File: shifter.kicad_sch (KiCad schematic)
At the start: 11 parts

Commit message: made the board double wide. rough ASIC and vreg placement.
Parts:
- D1: renamed from D3; symbol Device:D -> bitaxe:D
- D2: renamed from D1; symbol Device:D -> bitaxe:D
- D3: renamed from D4; symbol Device:D -> bitaxe:D
- D4: renamed from D2; symbol Device:D -> bitaxe:D
- renumbered C to C180, R29 to R33, R14 to R34, R32 to R35, R26 to R36, R27 to R37, R28 to R38
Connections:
- net RESET_IN: now also D3.A; no longer D3.2 (A)
- net RESET_OUT: now also D3.K; no longer D3.1 (K)
- net RX_IN: now also D4.A; no longer D4.2 (A)
- net RX_OUT: now also D4.K; no longer D4.1 (K)
- net TRIP_IN: now also D1.K; no longer D1.1 (K)
- net TRIP_OUT: now also D1.A; no longer D1.2 (A)
- net TX_IN: now also D2.K; no longer D2.1 (K)
- net TX_OUT: now also D2.A; no longer D2.2 (A)
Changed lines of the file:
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@@
 		(on_board yes)
 		(dnp no)
-		(property "Reference" "R29"
+		(property "Reference" "R33"
 			(at 102.87 111.76 0)
 			(effects
@@
 			(project "BitaxeBonanza"
 				(path "/61fe8d2c-9301-4ad9-8caf-c47acfa835b0/5053a6d5-ae8d-4ae0-9f6e-0d65e80da719/0ebdc3ac-b196-4195-a4b9-cad7cca42700"
-					(reference "R29")
+					(reference "R33")
 					(unit 1)
 				)
 				(path "/61fe8d2c-9301-4ad9-8caf-c47acfa835b0/5053a6d5-ae8d-4ae0-9f6e-0d65e80da719/a86c111d-117d-4919-aa69-a196b04aa4d8"
-					(reference "R34")
+					(reference "R39")
 					(unit 1)
 				)
@@
 	)
 	(symbol
-		(lib_id "Device:D")
+		(lib_id "bitaxe:D")
 		(at 162.56 83.82 90)
 		(unit 1)
@@
 		(on_board yes)
 		(dnp no)
-		(property "Reference" "D2"
+		(property "Reference" "D4"
 			(at 161.29 80.518 0)
 			(effects
@@
 			)
 		)
-		(property "Datasheet" "https://fscdn.rohm.com/en/products/databook/datasheet/discrete/diode/switching/1ss380vmte-17-e.pdf"
+		(property "Datasheet" "~"
 			(at 162.56 83.82 0)
 			(effects
@@
 			)
 		)
-		(pin "1"
-		)
-		(pin "2"
-		)
-		(instances
-			(project "BitaxeBonanza"
-				(path "/61fe8d2c-9301-4ad9-8caf-c47acfa835b0/5053a6d5-ae8d-4ae0-9f6e-0d65e80da719/0ebdc3ac-b196-4195-a4b9-cad7cca42700"
-					(reference "D2")
+		(property "Sim.Device" "D"
+			(at 162.56 83.82 0)
+			(effects
+				(font
+					(size 1.27 1.27)
+				)
+				(hide yes)
+			)
+		)
+		(property "Sim.Pins" "1=K 2=A"
+			(at 162.56 83.82 0)
+			(effects
+				(font
+					(size 1.27 1.27)
+				)
+				(hide yes)
+			)
+		)
+		(pin "A"
+		)
+		(pin "K"
+		)
+		(instances
+			(project "BitaxeBonanza"
+				(path "/61fe8d2c-9301-4ad9-8caf-c47acfa835b0/5053a6d5-ae8d-4ae0-9f6e-0d65e80da719/0ebdc3ac-b196-4195-a4b9-cad7cca42700"
+					(reference "D4")
 					(unit 1)
 				)
@@
 		(dnp no)
 		(fields_autoplaced yes)
-		(property "Reference" "C"
+		(property "Reference" "C180"
 			(at 190.5 91.4335 0)
 			(effects
@@
 		(instances
 			(project "BitaxeBonanza"
+				(path "/61fe8d2c-9301-4ad9-8caf-c47acfa835b0/5053a6d5-ae8d-4ae0-9f6e-0d65e80da719/0ebdc3ac-b196-4195-a4b9-cad7cca42700"
+					(reference "C180")
+					(unit 1)
+				)
 				(path "/61fe8d2c-9301-4ad9-8caf-c47acfa835b0/5053a6d5-ae8d-4ae0-9f6e-0d65e80da719/a86c111d-117d-4919-aa69-a196b04aa4d8"
-					(reference "C50")
+					(reference "C181")
 					(unit 1)
 				)
 				(path "/61fe8d2c-9301-4ad9-8caf-c47acfa835b0/5053a6d5-ae8d-4ae0-9f6e-0d65e80da719/aedf8646-f124-43c2-a6e9-f307494e235d"
-					(reference "C51")
+					(reference "C182")
 					(unit 1)
 				)
@@
 		(on_board yes)
 		(dnp no)
-		(property "Reference" "R28"
+		(property "Reference" "R38"
 			(at 197.866 68.326 90)
 			(effects
@@
 			(project "BitaxeBonanza"
 				(path "/61fe8d2c-9301-4ad9-8caf-c47acfa835b0/5053a6d5-ae8d-4ae0-9f6e-0d65e80da719/0ebdc3ac-b196-4195-a4b9-cad7cca42700"
-					(reference "R28")
+					(reference "R38")
 					(unit 1)
 				)
@@
 	)
 	(symbol
-		(lib_id "Device:D")
+		(lib_id "bitaxe:D")
 		(at 93.98 83.82 90)
 		(unit 1)
@@
 		(on_board yes)
 		(dnp no)
-		(property "Reference" "D3"
+		(property "Reference" "D1"
 			(at 96.266 79.756 0)
 			(effects
@@
 			)
 		)
-		(property "Datasheet" "https://fscdn.rohm.com/en/products/databook/datasheet/discrete/diode/switching/1ss380vmte-17-e.pdf"
+		(property "Datasheet" "~"
 			(at 93.98 83.82 0)
 			(effects
@@
 			)
 		)
-		(pin "1"
-		)
-		(pin "2"
-		)
-		(instances
-			(project "BitaxeBonanza"
-				(path "/61fe8d2c-9301-4ad9-8caf-c47acfa835b0/5053a6d5-ae8d-4ae0-9f6e-0d65e80da719/0ebdc3ac-b196-4195-a4b9-cad7cca42700"
-					(reference "D3")
+		(property "Sim.Device" "D"
+			(at 93.98 83.82 0)
+			(effects
+				(font
+					(size 1.27 1.27)
+				)
+				(hide yes)
+			)
+		)
+		(property "Sim.Pins" "1=K 2=A"
+			(at 93.98 83.82 0)
+			(effects
+				(font
+					(size 1.27 1.27)
+				)
+				(hide yes)
+			)
+		)
+		(pin "A"
+		)
+		(pin "K"
+		)
+		(instances
+			(project "BitaxeBonanza"
+				(path "/61fe8d2c-9301-4ad9-8caf-c47acfa835b0/5053a6d5-ae8d-4ae0-9f6e-0d65e80da719/0ebdc3ac-b196-4195-a4b9-cad7cca42700"
+					(reference "D1")
 					(unit 1)
 				)
@@
 		(on_board yes)
 		(dnp no)
-		(property "Reference" "R14"
+		(property "Reference" "R34"
 			(at 120.65 91.186 0)
 			(effects
@@
 			(project "BitaxeBonanza"
 				(path "/61fe8d2c-9301-4ad9-8caf-c47acfa835b0/5053a6d5-ae8d-4ae0-9f6e-0d65e80da719/0ebdc3ac-b196-4195-a4b9-cad7cca42700"
-					(reference "R14")
+					(reference "R34")
 					(unit 1)
 				)
 				(path "/61fe8d2c-9301-4ad9-8caf-c47acfa835b0/5053a6d5-ae8d-4ae0-9f6e-0d65e80da719/a86c111d-117d-4919-aa69-a196b04aa4d8"
-					(reference "R36")
+					(reference "R40")
 					(unit 1)
 				)
@@
 	)
 	(symbol
-		(lib_id "Device:D")
+		(lib_id "bitaxe:D")
 		(at 139.7 83.82 90)
 		(unit 1)
@@
 		(on_board yes)
 		(dnp no)
-		(property "Reference" "D4"
+		(property "Reference" "D3"
 			(at 141.478 80.518 0)
 			(effects
@@
 			)
 		)
-		(property "Datasheet" "https://fscdn.rohm.com/en/products/databook/datasheet/discrete/diode/switching/1ss380vmte-17-e.pdf"
+		(property "Datasheet" "~"
 			(at 139.7 83.82 0)
 			(effects
@@
 			)
 		)
-		(pin "1"
-		)
-		(pin "2"
-		)
-		(instances
-			(project "BitaxeBonanza"
-				(path "/61fe8d2c-9301-4ad9-8caf-c47acfa835b0/5053a6d5-ae8d-4ae0-9f6e-0d65e80da719/0ebdc3ac-b196-4195-a4b9-cad7cca42700"
-					(reference "D4")
+		(property "Sim.Device" "D"
+			(at 139.7 83.82 0)
+			(effects
+				(font
+					(size 1.27 1.27)
+				)
+				(hide yes)
+			)
+		)
+		(property "Sim.Pins" "1=K 2=A"
+			(at 139.7 83.82 0)
+			(effects
+				(font
+					(size 1.27 1.27)
+				)
+				(hide yes)
+			)
+		)
+		(pin "K"
+		)
+		(pin "A"
+		)
+		(instances
+			(project "BitaxeBonanza"
+				(path "/61fe8d2c-9301-4ad9-8caf-c47acfa835b0/5053a6d5-ae8d-4ae0-9f6e-0d65e80da719/0ebdc3ac-b196-4195-a4b9-cad7cca42700"
+					(reference "D3")
 					(unit 1)
 				)
@@
 		(on_board yes)
 		(dnp no)
-		(property "Reference" "R32"
+		(property "Reference" "R35"
 			(at 145.034 66.04 0)
 			(effects
@@
 			(project "BitaxeBonanza"
 				(path "/61fe8d2c-9301-4ad9-8caf-c47acfa835b0/5053a6d5-ae8d-4ae0-9f6e-0d65e80da719/0ebdc3ac-b196-4195-a4b9-cad7cca42700"
-					(reference "R32")
+					(reference "R35")
 					(unit 1)
 				)
@@
 	)
 	(symbol
-		(lib_id "Device:D")
+		(lib_id "bitaxe:D")
 		(at 128.27 83.82 90)
 		(unit 1)
@@
 		(on_board yes)
 		(dnp no)
-		(property "Reference" "D1"
+		(property "Reference" "D2"
 			(at 130.048 80.01 0)
 			(effects
@@
 			)
 		)
-		(property "Datasheet" "https://fscdn.rohm.com/en/products/databook/datasheet/discrete/diode/switching/1ss380vmte-17-e.pdf"
+		(property "Datasheet" "~"
 			(at 128.27 83.82 0)
 			(effects
@@
 			)
 		)
-		(pin "1"
-		)
-		(pin "2"
-		)
-		(instances
-			(project "BitaxeBonanza"
-				(path "/61fe8d2c-9301-4ad9-8caf-c47acfa835b0/5053a6d5-ae8d-4ae0-9f6e-0d65e80da719/0ebdc3ac-b196-4195-a4b9-cad7cca42700"
-					(reference "D1")
+		(property "Sim.Device" "D"
+			(at 128.27 83.82 0)
+			(effects
+				(font
+					(size 1.27 1.27)
+				)
+				(hide yes)
+			)
+		)
+		(property "Sim.Pins" "1=K 2=A"
+			(at 128.27 83.82 0)
+			(effects
+				(font
+					(size 1.27 1.27)
+				)
+				(hide yes)
+			)
+		)
+		(pin "K"
+		)
+		(pin "A"
+		)
+		(instances
+			(project "BitaxeBonanza"
+				(path "/61fe8d2c-9301-4ad9-8caf-c47acfa835b0/5053a6d5-ae8d-4ae0-9f6e-0d65e80da719/0ebdc3ac-b196-4195-a4b9-cad7cca42700"
+					(reference "D2")
 					(unit 1)
 				)
@@
 		(on_board yes)
 		(dnp no)
-		(property "Reference" "R26"
+		(property "Reference" "R36"
 			(at 167.894 66.04 0)
 			(effects
@@
 			(project "BitaxeBonanza"
 				(path "/61fe8d2c-9301-4ad9-8caf-c47acfa835b0/5053a6d5-ae8d-4ae0-9f6e-0d65e80da719/0ebdc3ac-b196-4195-a4b9-cad7cca42700"
-					(reference "R26")
+					(reference "R36")
 					(unit 1)
 				)
@@
 		(on_board yes)
 		(dnp no)
-		(property "Reference" "R27"
+		(property "Reference" "R37"
 			(at 198.12 50.8 90)
 			(effects
@@
 			(project "BitaxeBonanza"
 				(path "/61fe8d2c-9301-4ad9-8caf-c47acfa835b0/5053a6d5-ae8d-4ae0-9f6e-0d65e80da719/0ebdc3ac-b196-4195-a4b9-cad7cca42700"
-					(reference "R27")
-					(unit 1)
-				)
+					(reference "R37")
+					(unit 1)
+				)

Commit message: added gerbers and BOM
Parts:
- C180: DK (none) -> 490-1303-1-ND; PARTNO (none) -> GRM155R71H102KA01D
- R33, R34, R35, R36, R37, R38: DK (none) -> 311-1.0KJRCT-ND; PARTNO (none) -> RC0402JR-071KL
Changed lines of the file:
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@@
+			)
+		)
+		(property "DK" "311-1.0KJRCT-ND"
+			(at 99.06 113.03 0)
+			(effects
+				(font
+					(size 1.27 1.27)
+				)
+			)
+		)
+		(property "PARTNO" "RC0402JR-071KL"
+			(at 99.06 113.03 0)
+			(effects
+				(font
+					(size 1.27 1.27)
+				)
 			)
 		)
@@
 			)
 		)
+		(property "DK" "490-1303-1-ND"
+			(at 187.96 92.71 0)
+			(effects
+				(font
+					(size 1.27 1.27)
+				)
+			)
+		)
+		(property "PARTNO" "GRM155R71H102KA01D"
+			(at 187.96 92.71 0)
+			(effects
+				(font
+					(size 1.27 1.27)
+				)
+			)
+		)
 		(pin "1"
 		)
@@
 				)
 				(hide yes)
+			)
+		)
+		(property "DK" "311-1.0KJRCT-ND"
+			(at 193.04 68.58 0)
+			(effects
+				(font
+					(size 1.27 1.27)
+				)
+			)
+		)
+		(property "PARTNO" "RC0402JR-071KL"
+			(at 193.04 68.58 0)
+			(effects
+				(font
+					(size 1.27 1.27)
+				)
 			)
 		)
@@
 			)
 		)
+		(property "DK" "311-1.0KJRCT-ND"
+			(at 121.92 92.71 0)
+			(effects
+				(font
+					(size 1.27 1.27)
+				)
+			)
+		)
+		(property "PARTNO" "RC0402JR-071KL"
+			(at 121.92 92.71 0)
+			(effects
+				(font
+					(size 1.27 1.27)
+				)
+			)
+		)
 		(pin "2"
 		)
@@
 			)
 		)
+		(property "DK" "311-1.0KJRCT-ND"
+			(at 143.51 67.31 0)
+			(effects
+				(font
+					(size 1.27 1.27)
+				)
+			)
+		)
+		(property "PARTNO" "RC0402JR-071KL"
+			(at 143.51 67.31 0)
+			(effects
+				(font
+					(size 1.27 1.27)
+				)
+			)
+		)
 		(pin "2"
 		)
@@
 			)
 		)
+		(property "DK" "311-1.0KJRCT-ND"
+			(at 166.37 67.31 0)
+			(effects
+				(font
+					(size 1.27 1.27)
+				)
+			)
+		)
+		(property "PARTNO" "RC0402JR-071KL"
+			(at 166.37 67.31 0)
+			(effects
+				(font
+					(size 1.27 1.27)
+				)
+			)
+		)
 		(pin "2"
 		)
@@
 			)
 		)
+		(property "DK" "311-1.0KJRCT-ND"
+			(at 193.04 50.8 0)
+			(effects
+				(font
+					(size 1.27 1.27)
+				)
+			)
+		)
+		(property "PARTNO" "RC0402JR-071KL"
+			(at 193.04 50.8 0)
+			(effects
+				(font
+					(size 1.27 1.27)
+				)
+			)
+		)

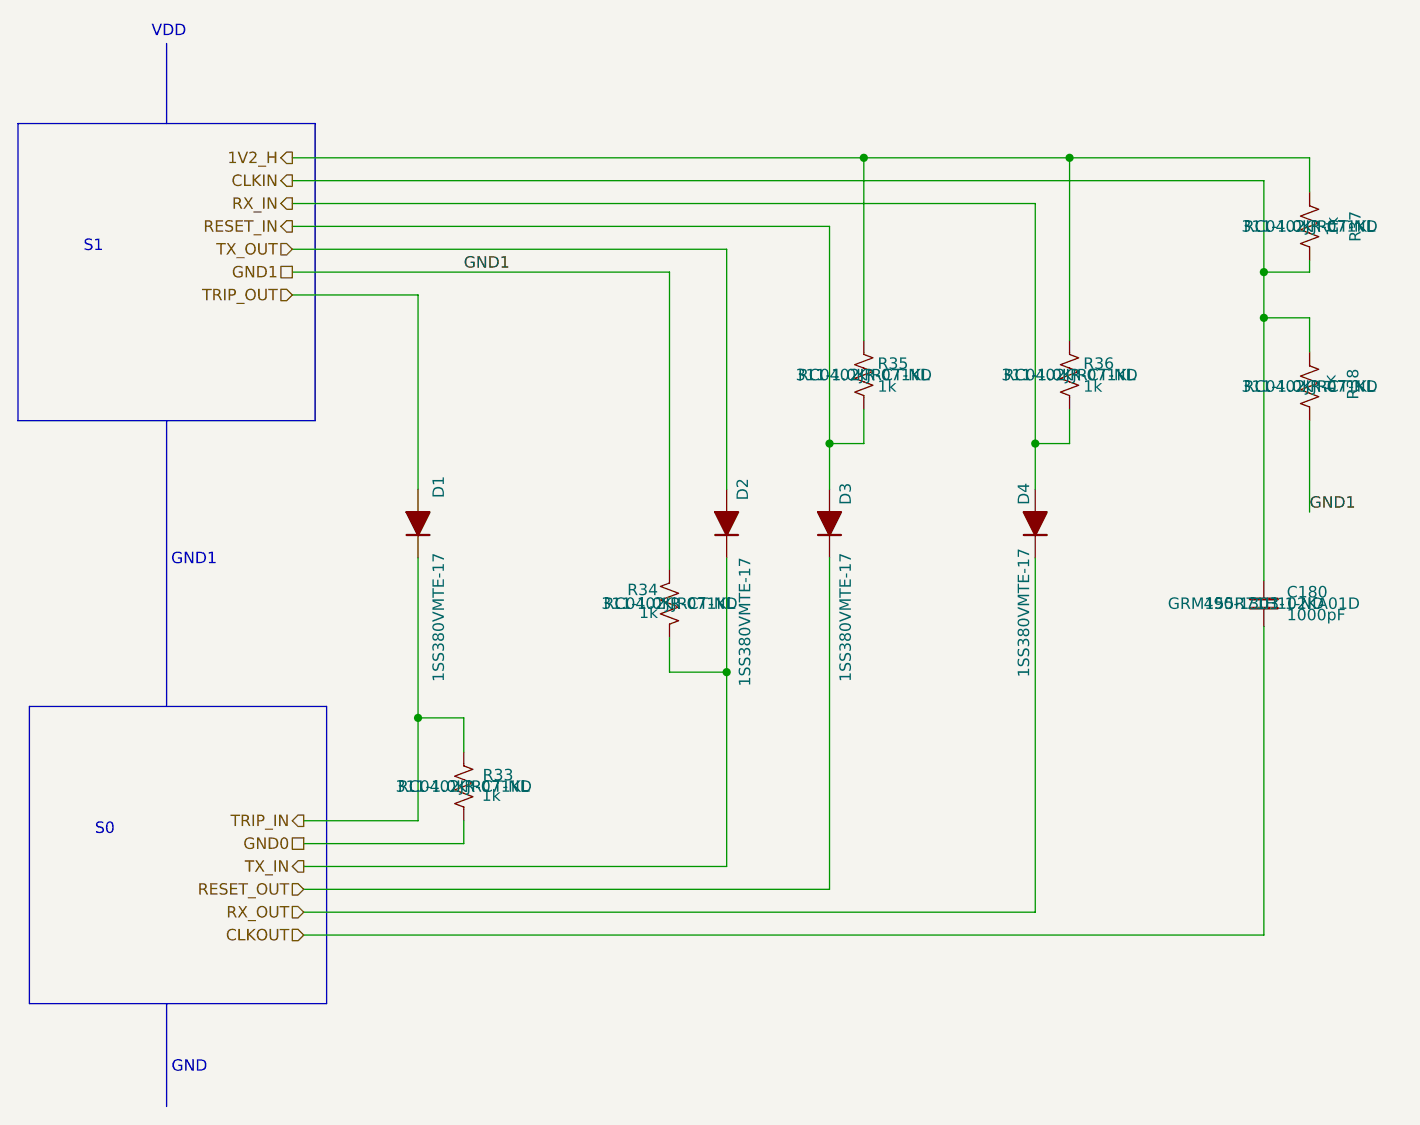
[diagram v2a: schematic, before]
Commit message: switch to the bitaxeBIRDS based pre-bonanza
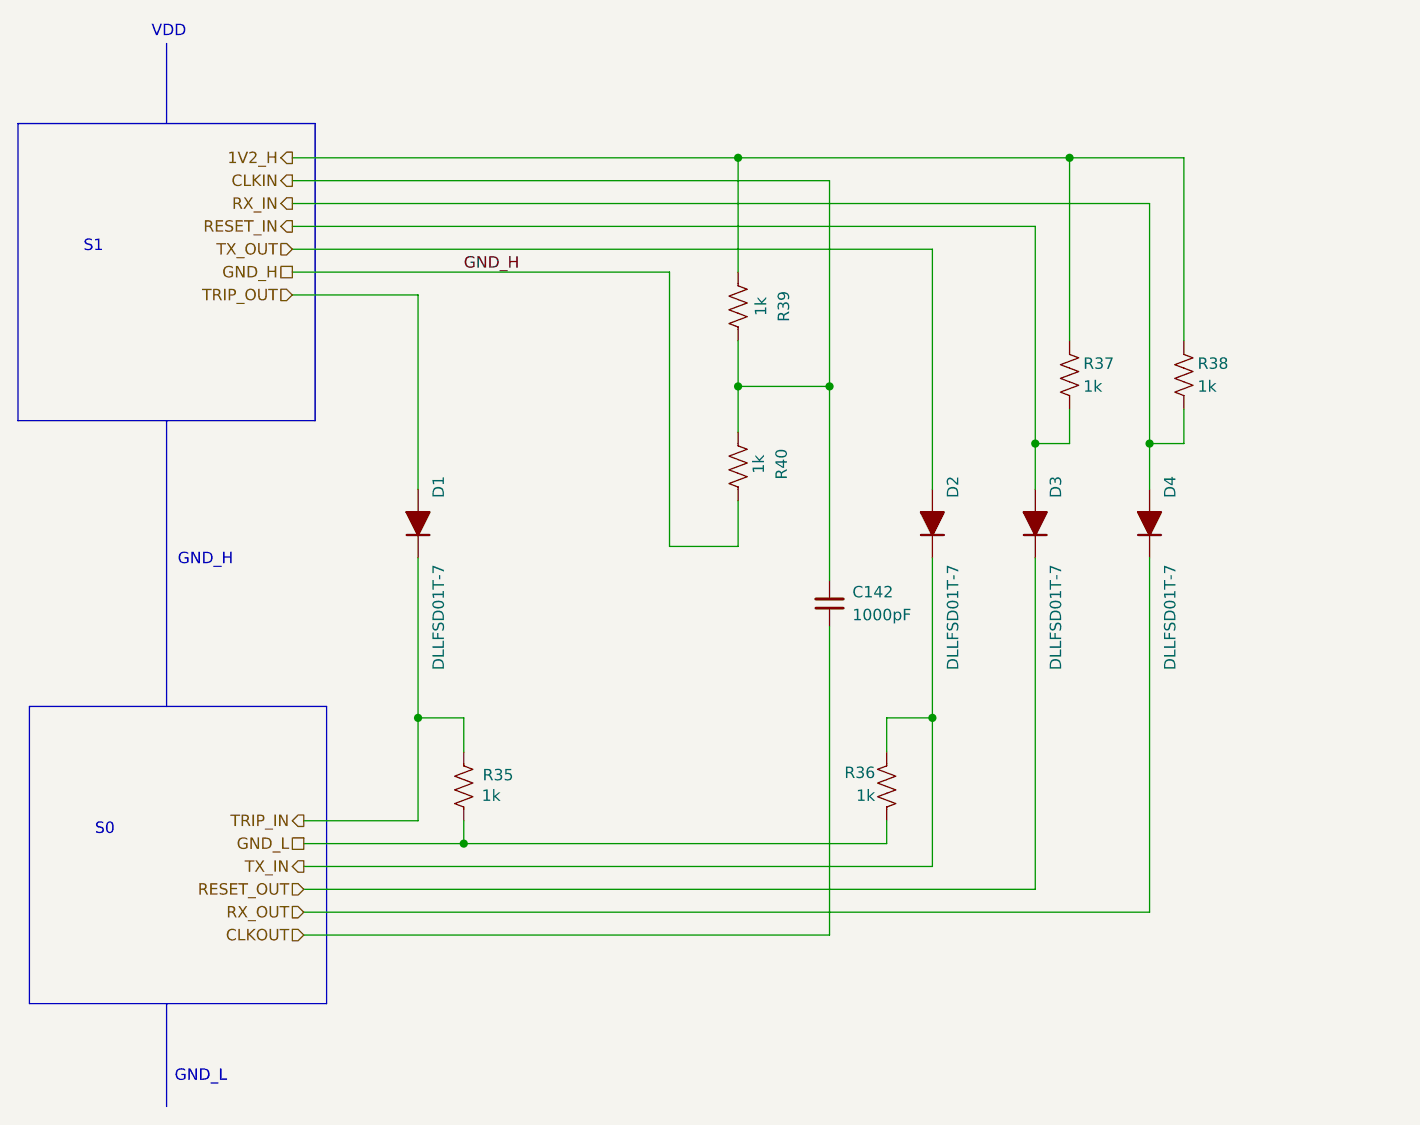
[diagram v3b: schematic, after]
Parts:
- D1, D2, D3, D4: value 1SS380VMTE-17 -> DLLFSD01T-7; footprint bitaxe:SOD-323FLUMD2_ROM -> bitaxe:D_SOD-523; DK 846-1SS380VMTE-17CT-ND -> DLLFSD01T-7DICT-ND; PARTNO 1SS380VMTE-17 -> DLLFSD01T-7
- R35: renamed from R33; DK 311-1.0KJRCT-ND -> 311-1.00KLRCT-ND; PARTNO RC0402JR-071KL -> RC0402FR-071KL
- R36: renamed from R34; DK 311-1.0KJRCT-ND -> 311-1.00KLRCT-ND; PARTNO RC0402JR-071KL -> RC0402FR-071KL
- R37: renamed from R35; DK 311-1.0KJRCT-ND -> 311-1.00KLRCT-ND; PARTNO RC0402JR-071KL -> RC0402FR-071KL
- R38: renamed from R36; DK 311-1.0KJRCT-ND -> 311-1.00KLRCT-ND; PARTNO RC0402JR-071KL -> RC0402FR-071KL
- R39: renamed from R37; DK 311-1.0KJRCT-ND -> 311-1.00KLRCT-ND; PARTNO RC0402JR-071KL -> RC0402FR-071KL
- R40: renamed from R38; DK 311-1.0KJRCT-ND -> 311-1.00KLRCT-ND; PARTNO RC0402JR-071KL -> RC0402FR-071KL
- renumbered C180 to C142
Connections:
- net TX_IN: now also R36.1; no longer R36.2
- net GND0 renamed GND_L
- net GND_L: now also R36.2
- net GND1 renamed GND_H
- net GND_H: no longer R36.1
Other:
- note added: "GND_H"
- note added: "GND_L"
- note removed: "GND"
- note removed: "GND1"
- title: (none) -> bitaxeBonanza
- moved on the sheet: C142, D2, D3, D4, R36, R37, R38, R39, R40

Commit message: updated schematic worksheet
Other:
- company: (none) -> bitaxeorg
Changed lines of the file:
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@@
 		(date "2026-02-11")
 		(rev "1002x")
+		(company "bitaxeorg")
+		(comment 1 "OHL v2")
 	)
 	(rectangle
